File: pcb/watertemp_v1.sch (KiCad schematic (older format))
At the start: 26 parts, among them J1 CONN_02X10, U1 LPC11U24FBD48, U2 LP5907-Q1, U3 RN2483, U4 SHT21, U5 DS18B20, Y1 Crystal

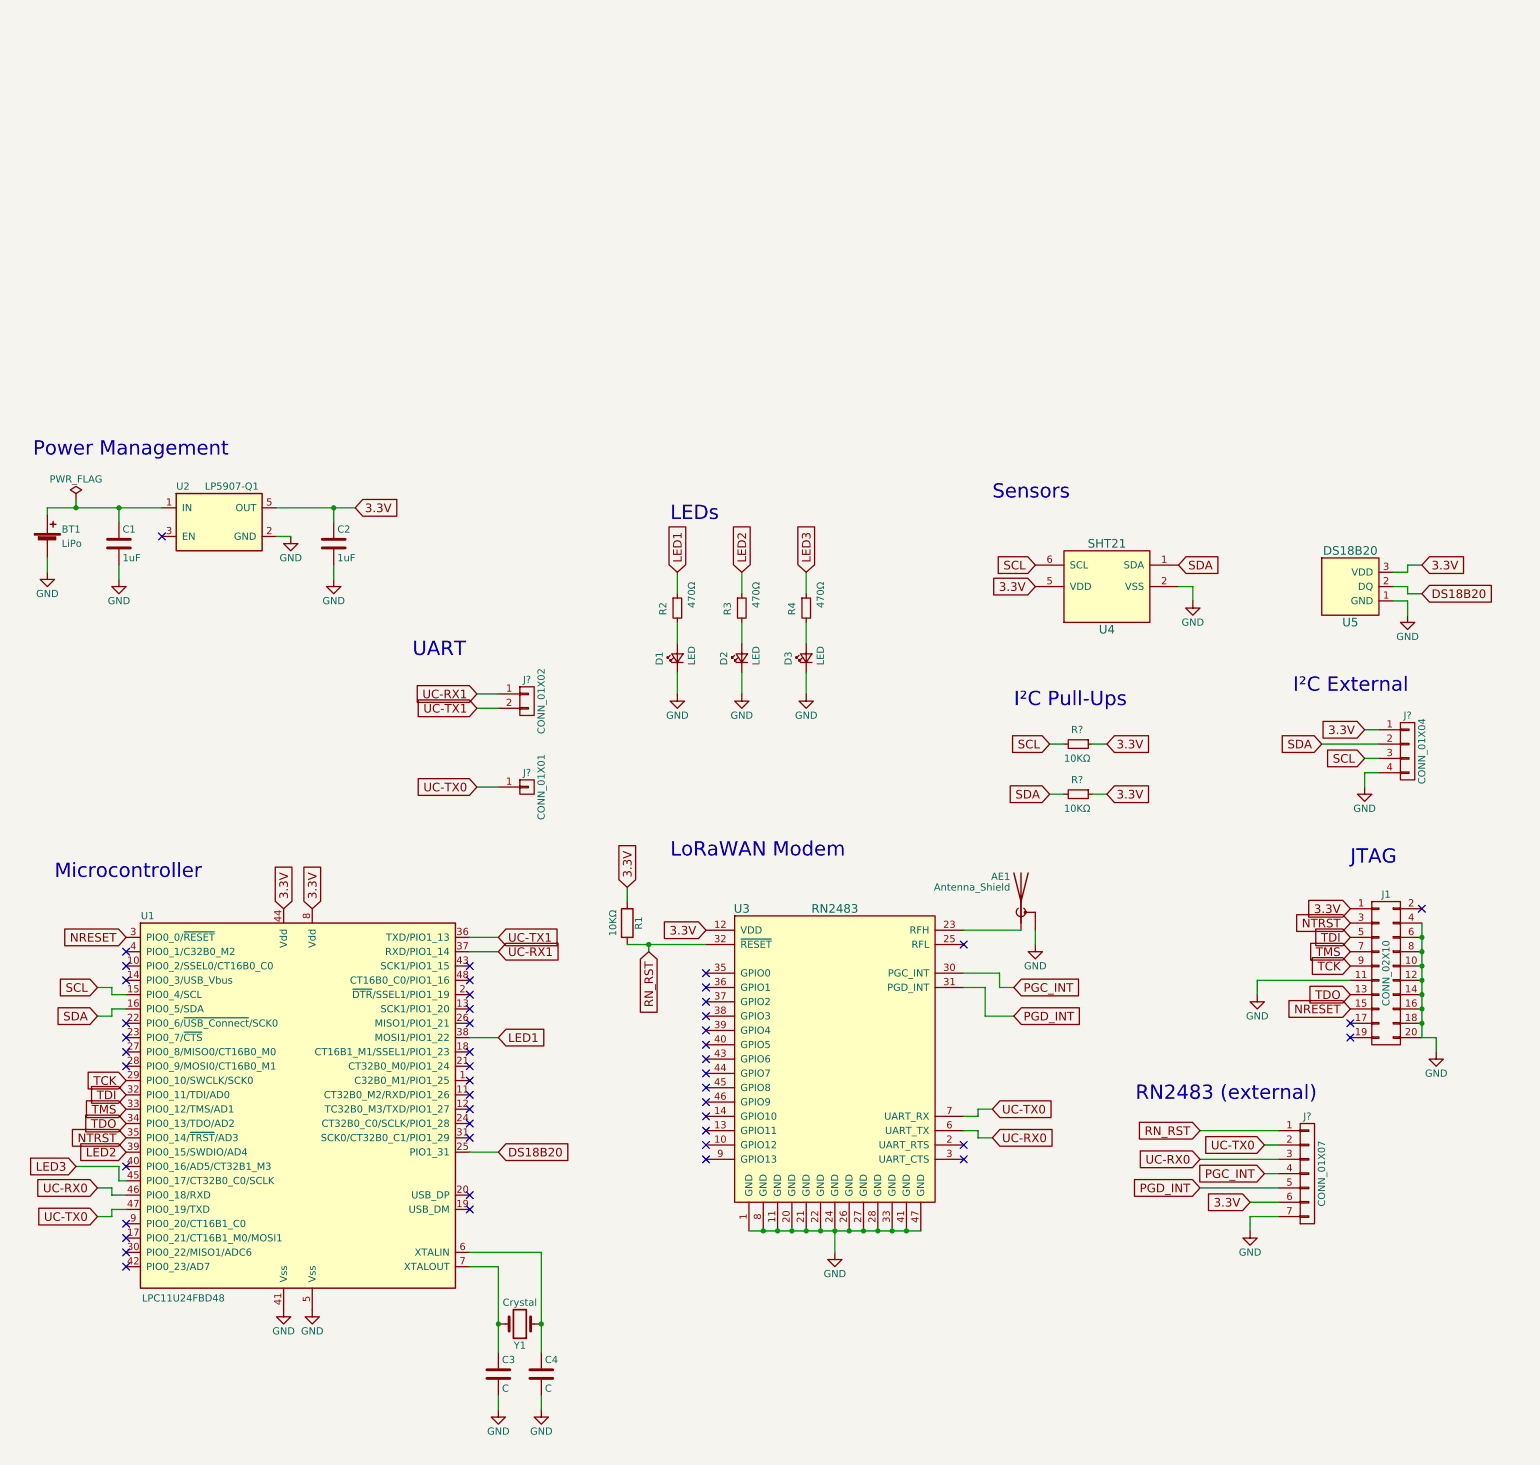
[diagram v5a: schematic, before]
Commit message: Reorganize schematics
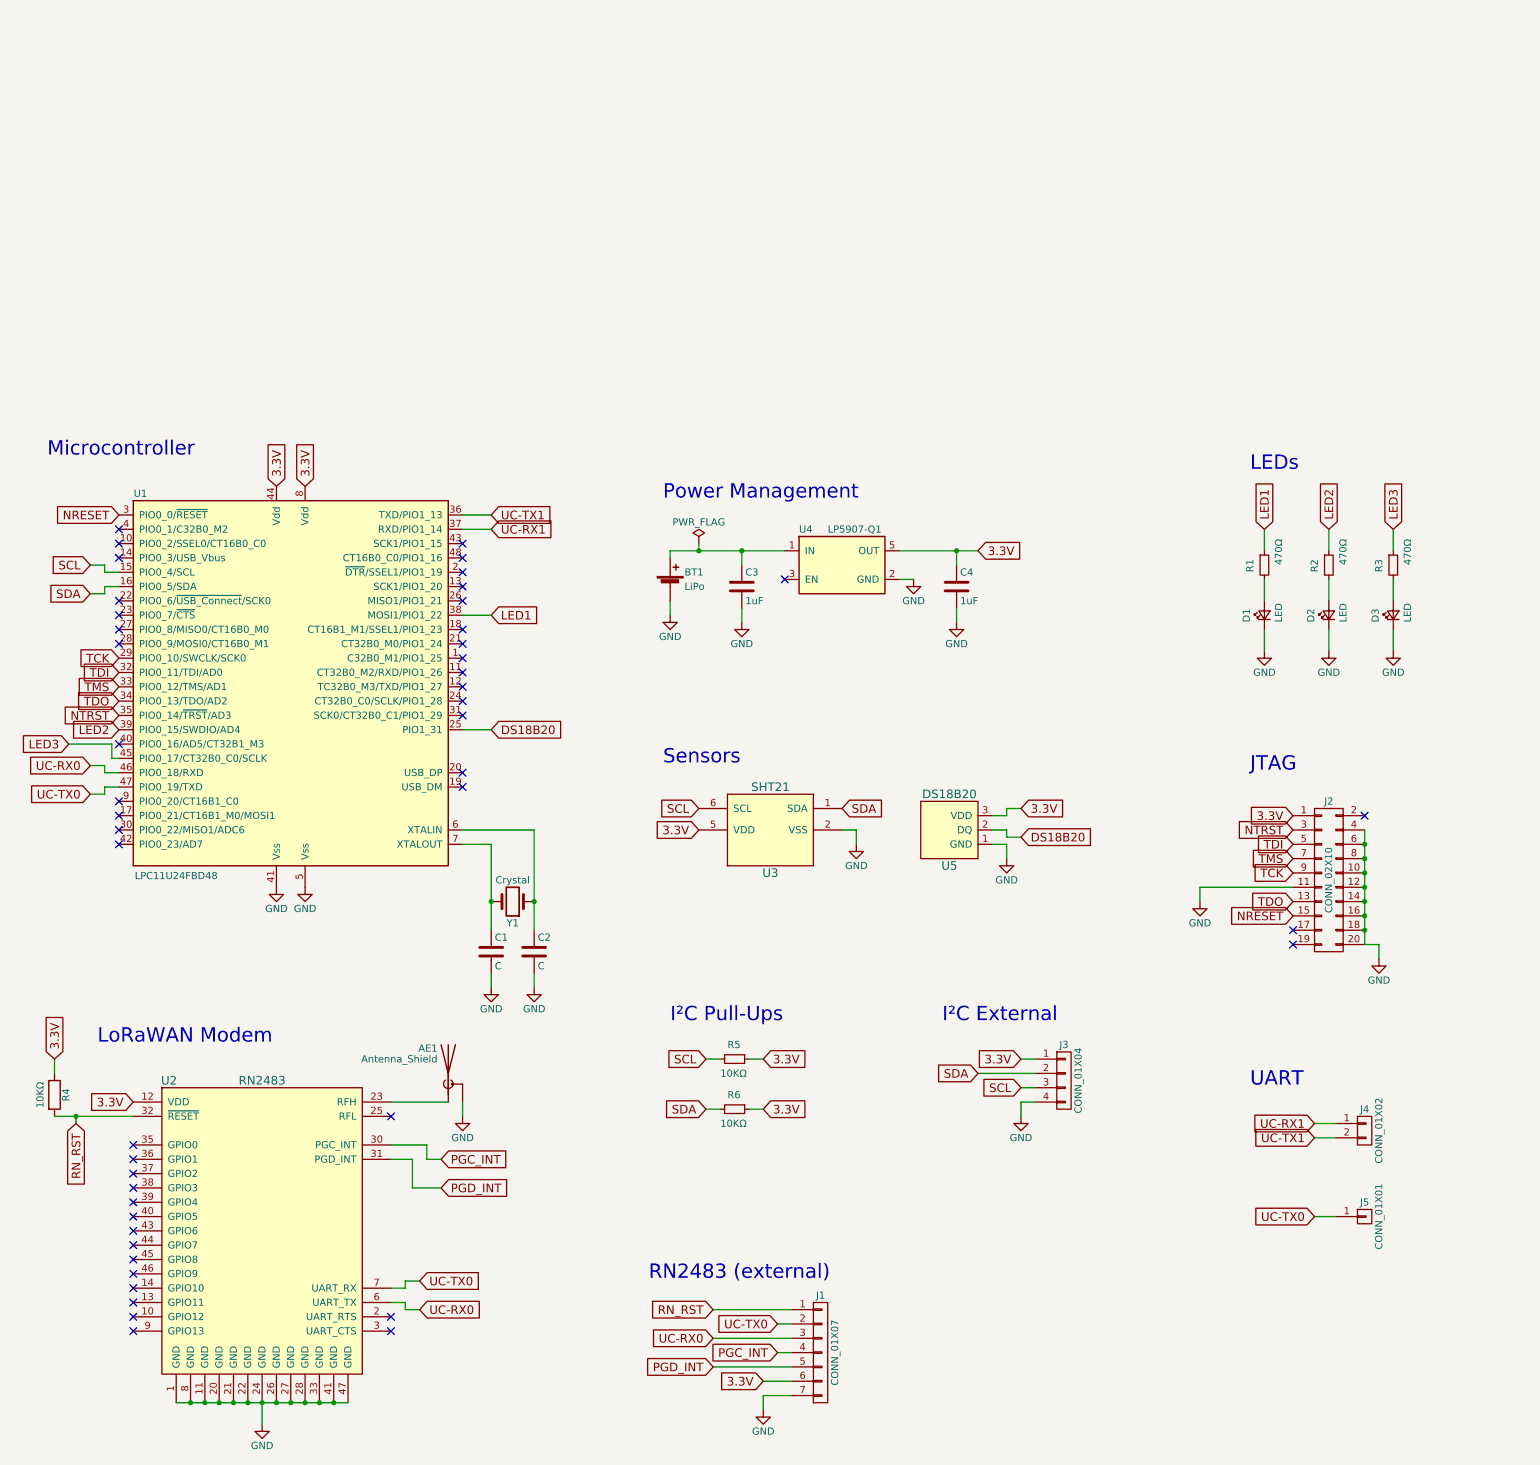
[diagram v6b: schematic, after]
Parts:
- gave numbers to parts that had none: 6
- renumbered C3 to C1, C4 to C2, C1 to C3, C2 to C4, J1 to J2, R2 to R1, R3 to R2, R4 to R3, R1 to R4, U3 to U2, U4 to U3, U2 to U4
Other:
- moved on the sheet: AE1, BT1, C1, C2, C3, C4, D1, D2, D3, J1, J2, J3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

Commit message: Finish parts selection
- Replace 20 pin JTAG connector with 10 pin SWD connector
- Choose footprints for all parts
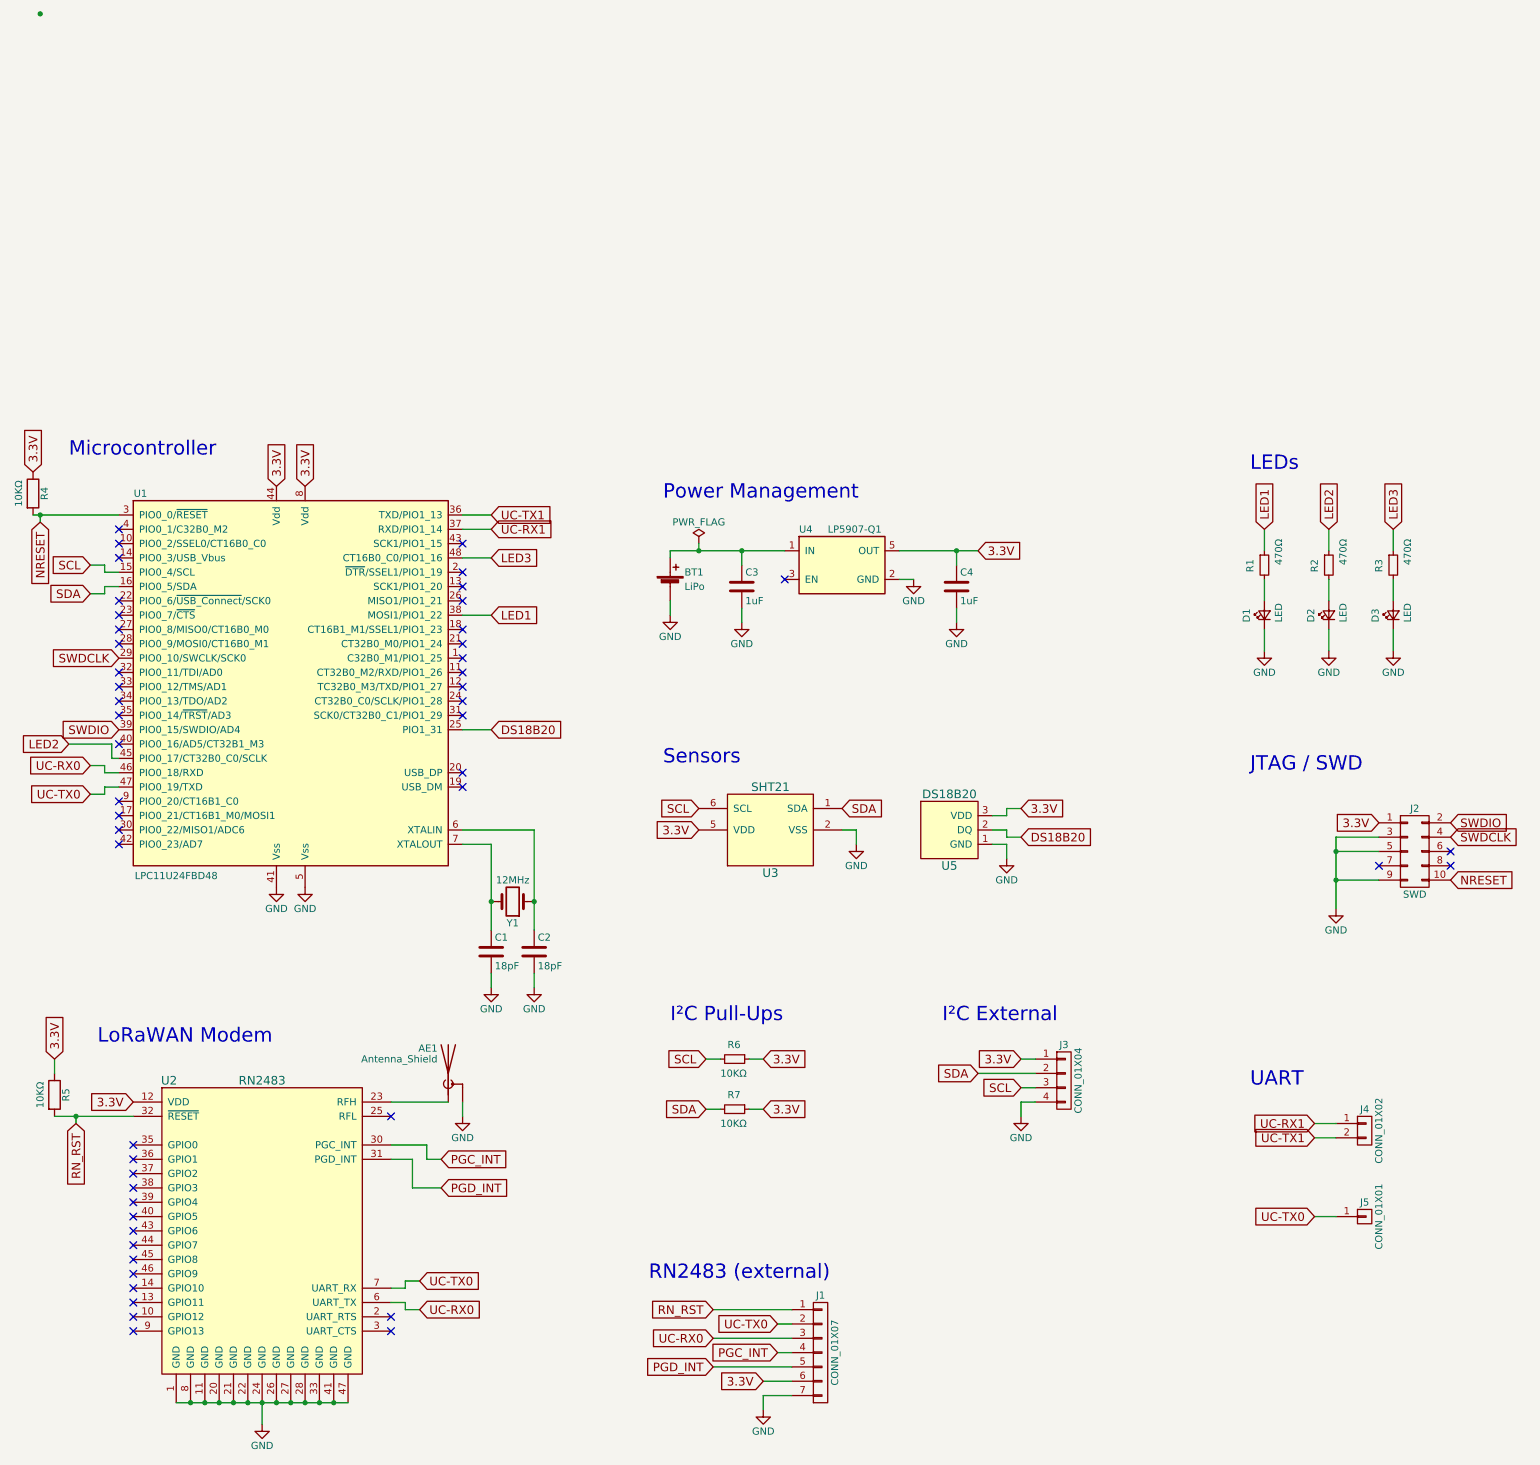
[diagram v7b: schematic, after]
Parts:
- removed J2: CONN_02X10, symbol CONN_02X10
- added J2: SWD, SWD:SWD_10Pin, symbol CONN_02X05
- added R4: 10KΩ, Resistors_SMD:R_1206_HandSoldering, symbol R
- AE1: footprint (none) -> RF:SMA_EDGE; Digikey (none) -> J502-ND
- BT1: footprint (none) -> Connectors_JST:JST_PH_B2B-PH-SM4-TB_02x2.00mm_Straight; Digikey (none) -> 455-1734-1-ND
- C1, C2: value C -> 18pF; footprint (none) -> Capacitors_SMD:C_0805; Digikey (none) -> 1276-1107-1-ND; Part (none) -> Samsung CL21C180JBANNNC
- C3: footprint (none) -> Capacitors_SMD:C_0805; Digikey (none) -> 1276-6471-1-ND; Part (none) -> Samsung CL21B105KOFNNNG
- C4: footprint (none) -> Capacitors_SMD:C_0805; Digikey (none) -> 1276-6471-1-ND; Part (none) -> Samsung Samsung CL21B105KOFNNNG
- D1, D2, D3: footprint (none) -> LEDs:LED_0805
- J1: footprint (none) -> Pin_Headers:Pin_Header_Straight_1x07_Pitch2.54mm
- J3: footprint (none) -> Pin_Headers:Pin_Header_Straight_1x04_Pitch2.54mm
- J4: footprint (none) -> Pin_Headers:Pin_Header_Straight_1x02_Pitch2.54mm
- J5: footprint (none) -> Pin_Headers:Pin_Header_Straight_1x01_Pitch2.54mm
- R1, R2, R3: footprint (none) -> Resistors_SMD:R_0805_HandSoldering
- R5: renamed from R4; footprint (none) -> Resistors_SMD:R_1206_HandSoldering
- R6: renamed from R5; footprint (none) -> Resistors_SMD:R_1206_HandSoldering
- R7: renamed from R6; footprint (none) -> Resistors_SMD:R_1206_HandSoldering
- U2: footprint (none) -> RN2483:RN2483
- U3: footprint (none) -> Sensirion:SHT21
- U5: footprint (none) -> Pin_Headers:Pin_Header_Straight_1x03_Pitch2.54mm
- Y1: value Crystal -> 12MHz; footprint (none) -> Crystals:Crystal_SMD_5032-2pin_5.0x3.2mm; Digikey (none) -> CTX1435CT-ND; Part (none) -> CTS 445C35A12M00000
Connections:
- net 3.3V: now also J2.1 (P1), R4.1
- net GND: now also J2.3 (P3), J2.5 (P5), J2.9 (P9)
- net LED2: now also U1.45 (PIO0_17/CT32B0_C0/SCLK); no longer U1.39 (PIO0_15/SWDIO/AD4)
- net LED3: now also U1.48 (CT16B0_C0/PIO1_16); no longer U1.45 (PIO0_17/CT32B0_C0/SCLK)
- net NRESET: now also J2.10 (P10), R4.2
- net NTRST: no longer names the net of U1.35 (PIO0_14/~TRST~/AD3)
- net TCK renamed SWDCLK
- net SWDCLK: now also J2.4 (P4)
- net TDI: no longer names the net of U1.32 (PIO0_11/TDI/AD0)
- net TDO: no longer names the net of U1.34 (PIO0_13/TDO/AD2)
- net TMS: no longer names the net of U1.33 (PIO0_12/TMS/AD1)
- new net SWDIO: J2.2 (P2), U1.39 (PIO0_15/SWDIO/AD4)
- no-connect marks 47 -> 50
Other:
- note added: "JTAG / SWD"
- note removed: "JTAG"

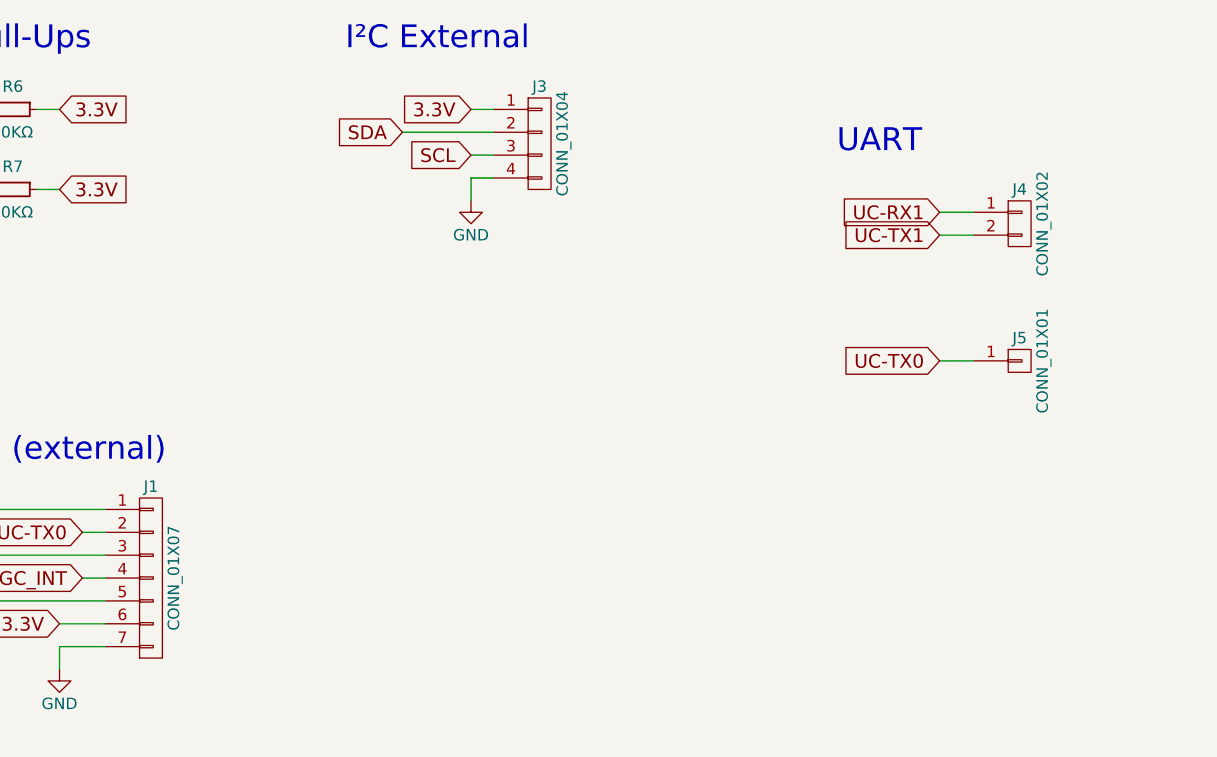
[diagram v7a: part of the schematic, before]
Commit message: Expose both UARTs
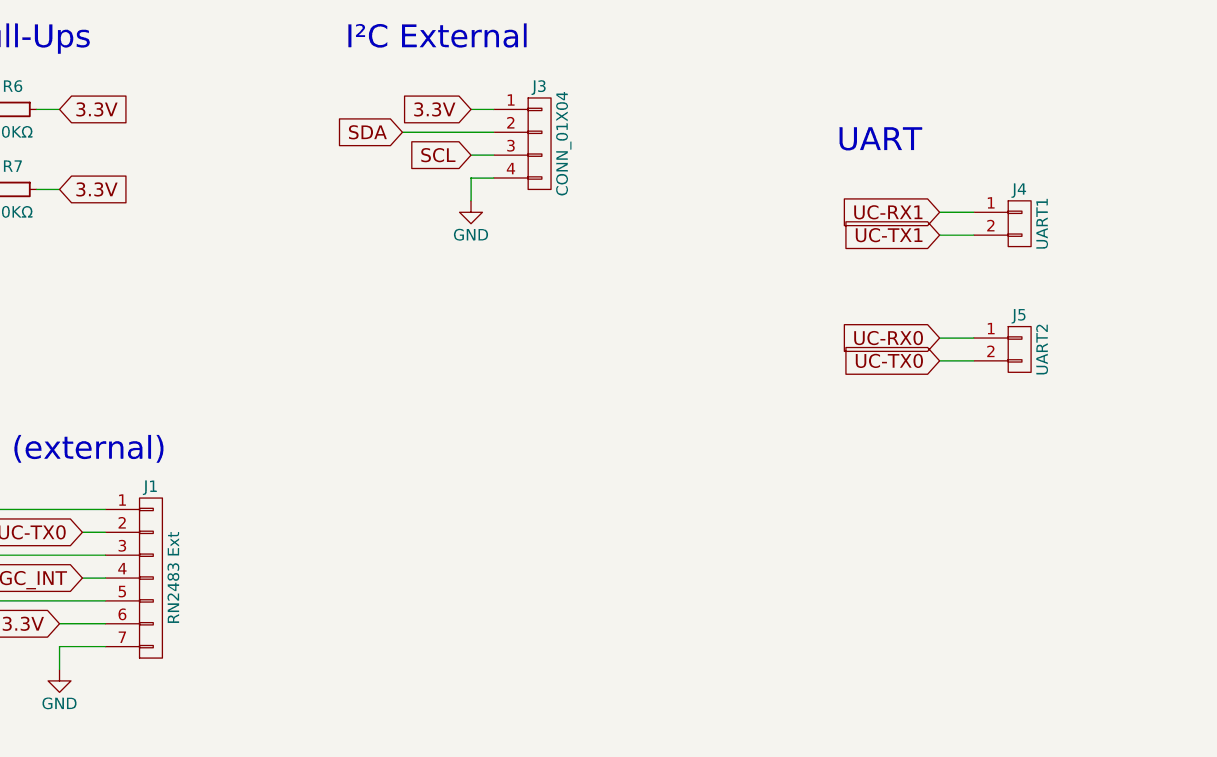
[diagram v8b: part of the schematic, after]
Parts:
- removed J5: CONN_01X01, Pin_Headers:Pin_Header_Straight_1x01_Pitch2.54mm, symbol CONN_01X01
- added J5: UART2, Pin_Headers:Pin_Header_Straight_1x02_Pitch2.54mm, symbol CONN_01X02
- J1: value CONN_01X07 -> RN2483 Ext
- J4: value CONN_01X02 -> UART1
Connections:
- net UC-RX0: now also J5.1 (P1)
- net UC-TX0: now also J5.2 (P2)
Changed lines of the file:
@@
 P 9950 5450
 F 0 "J4" H 9950 5600 50  0000 C CNN
-F 1 "CONN_01X02" V 10050 5450 50  0000 C CNN
+F 1 "UART1" V 10050 5450 50  0000 C CNN
 F 2 "Pin_Headers:Pin_Header_Straight_1x02_Pitch2.54mm" H 9950 5450 50  0001 C CNN
 F 3 "" H 9950 5450 50  0001 C CNN
@@
 Wire Wire Line
 	9750 5500 9600 5500
-$Comp
-L CONN_01X01 J5
-U 1 1 5973F46D
-P 9950 6050
-F 0 "J5" H 9950 6150 50  0000 C CNN
-F 1 "CONN_01X01" V 10050 6050 50  0000 C CNN
-F 2 "Pin_Headers:Pin_Header_Straight_1x01_Pitch2.54mm" H 9950 6050 50  0001 C CNN
-F 3 "" H 9950 6050 50  0001 C CNN
-	1    9950 6050
-	1    0    0    -1
-$EndComp
 Wire Wire Line
 	9750 6050 9600 6050
@@
 P 6150 7000
 F 0 "J1" H 6150 7400 50  0000 C CNN
-F 1 "CONN_01X07" V 6250 7000 50  0000 C CNN
+F 1 "RN2483 Ext" V 6250 7000 50  0000 C CNN
 F 2 "Pin_Headers:Pin_Header_Straight_1x07_Pitch2.54mm" H 6150 7000 50  0001 C CNN
 F 3 "" H 6150 7000 50  0001 C CNN
@@
 NoConn ~ 10550 3500
 Connection ~ 700  -2350
+$Comp
+L CONN_01X02 J5
+U 1 1 5975D417
+P 9950 6000
+F 0 "J5" H 9950 6150 50  0000 C CNN
+F 1 "UART2" V 10050 6000 50  0000 C CNN
+F 2 "Pin_Headers:Pin_Header_Straight_1x02_Pitch2.54mm" H 9950 6000 50  0001 C CNN
+F 3 "" H 9950 6000 50  0001 C CNN
+	1    9950 6000
+	1    0    0    -1
+$EndComp
+Text GLabel 9600 5950 0    60   Input ~ 0
+UC-RX0
+Wire Wire Line
+	9600 5950 9750 5950
 $EndSCHEMATC
